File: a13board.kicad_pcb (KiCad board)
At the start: 4 copper layers, 122.3 x 91.1 mm, 147 parts, among them U1 H27UBG8T2A/TSOP48, U2 A13, U3 H5TQ2G43CFR, U4 H5TQ2G43CFR, U5 OLIMEX_IC_AXP209, U6 SY8008BAAC, U7 SY8008BAAC

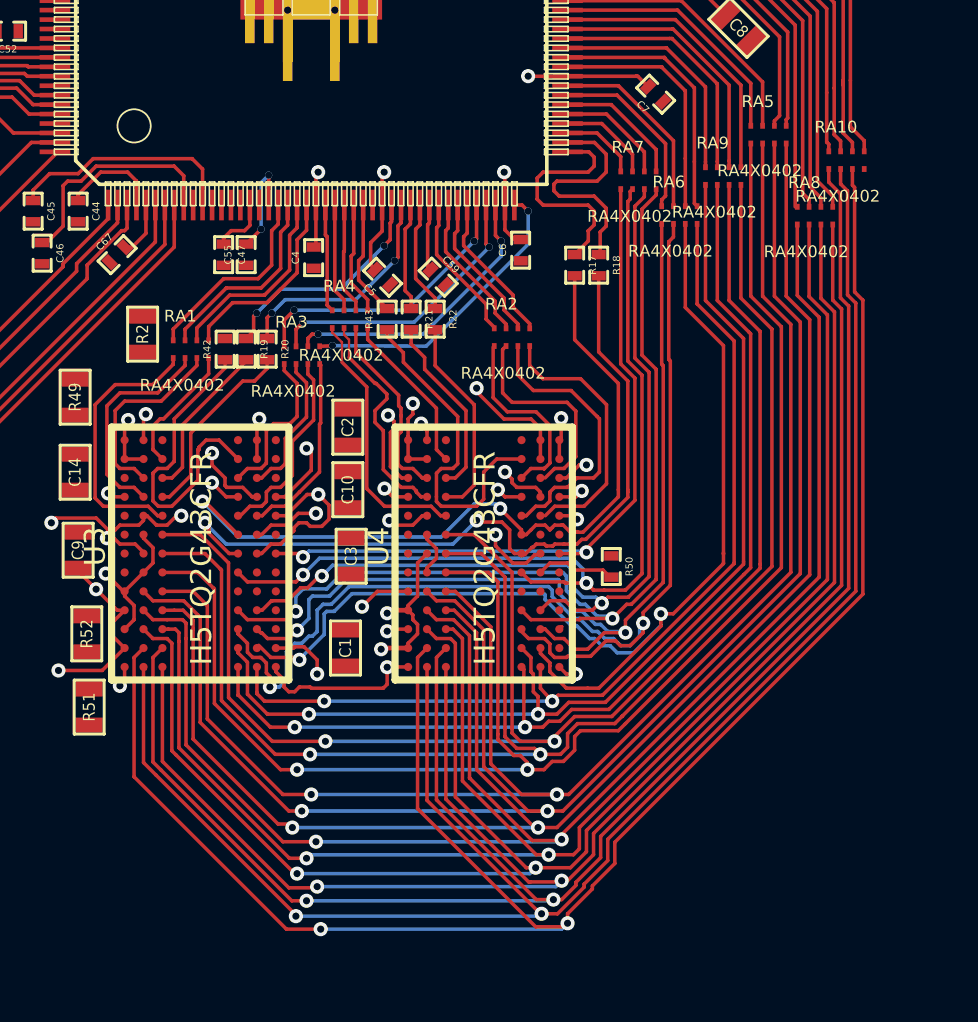
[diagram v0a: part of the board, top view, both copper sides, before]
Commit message: reducing space, occupied by address lines
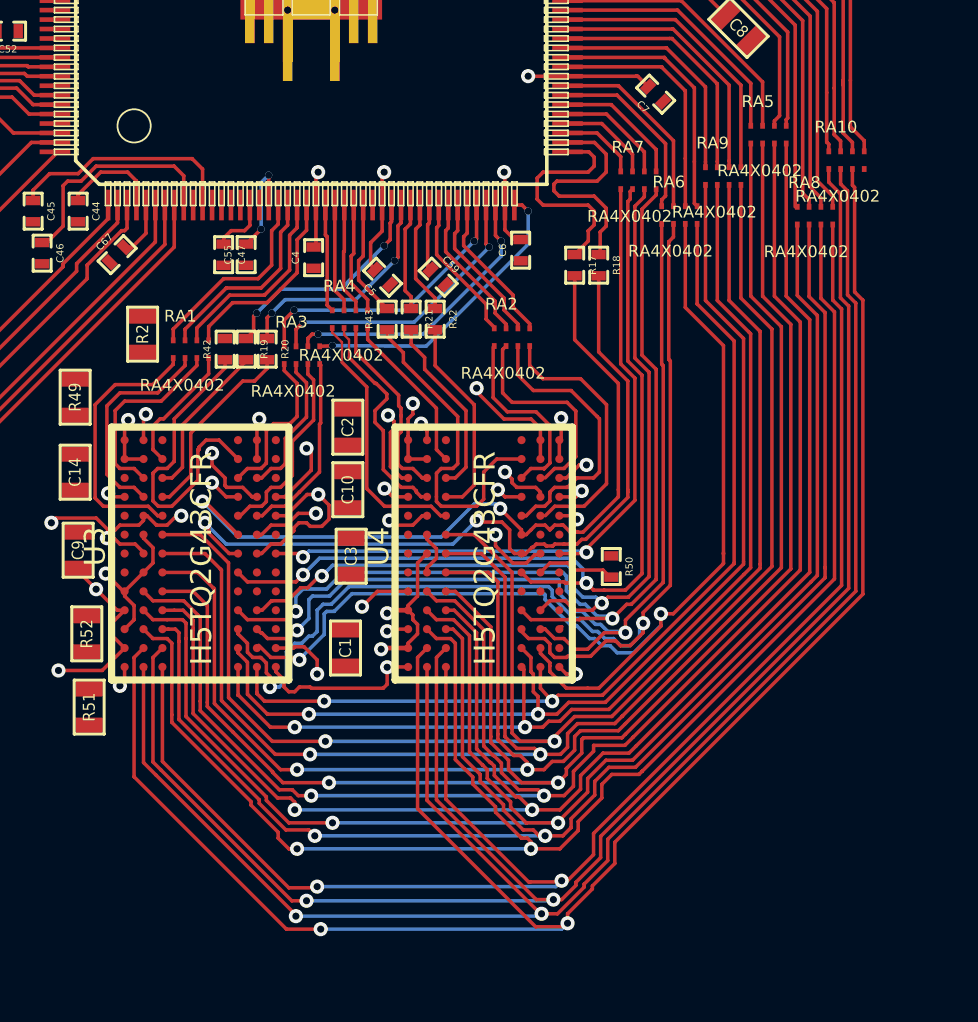
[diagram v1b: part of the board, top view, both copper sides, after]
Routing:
- net /DRAM/DDR3_A2: track 67.6 -> 65.3 mm
- net /DRAM/DDR3_A5: track 69.8 -> 67.6 mm
- net /DRAM/DDR3_A3: track 69.0 -> 67.1 mm
- net /DRAM/DDR3_A0: track 68.5 -> 66.9 mm
- net /DRAM/DDR3_BA0: track 69.4 -> 68.3 mm
- net /DRAM/DDR3_BA2: track 67.2 -> 66.4 mm

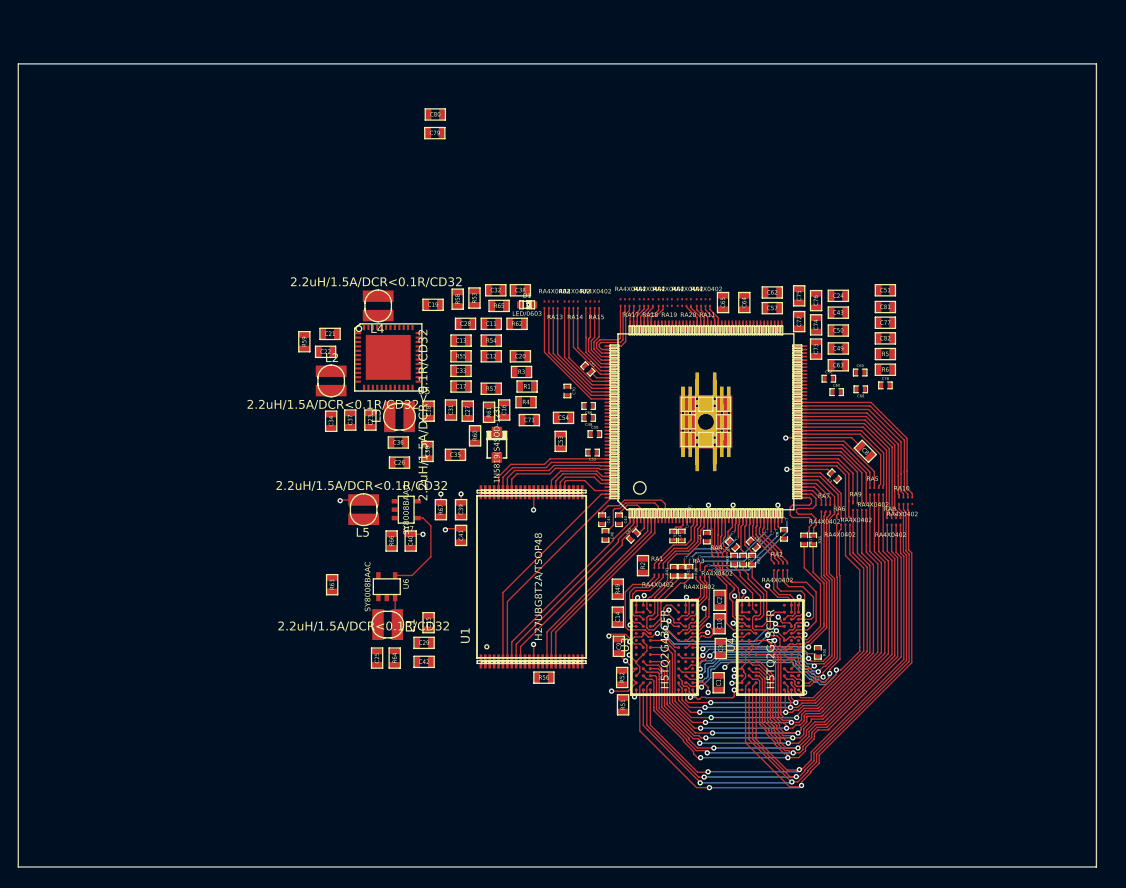
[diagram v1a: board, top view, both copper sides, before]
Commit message: Fixed some bugs with symbols, tracing continued
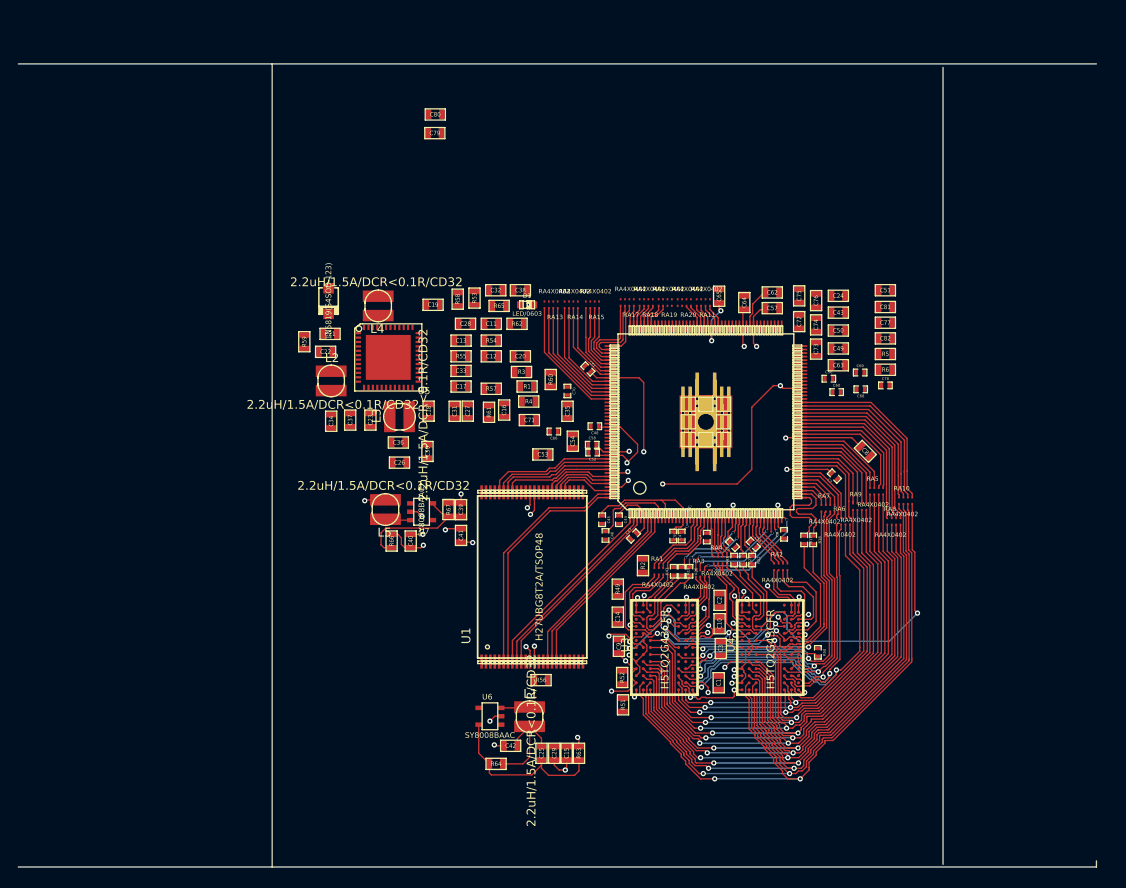
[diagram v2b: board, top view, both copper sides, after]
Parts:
- moved R63 33.9 mm to (99.1, 128.6), turned to 270 degrees
- moved D2 25.1 mm to (70.7, 77.3), turned to 90 degrees
- moved C15 21.6 mm to (97.7, 128.6), turned to 270 degrees
- moved C25 21.6 mm to (94.8, 128.6)
- moved C29 19.4 mm to (96.3, 128.6), turned to 90 degrees
- moved L1 19.2 mm to (93.5, 124.5), turned to 0 degrees
- moved U6 18.8 mm to (89.0, 124.4), turned to 90 degrees
- moved R64 16.6 mm to (89.7, 129.8), turned to 0 degrees
- moved C42 13.7 mm to (91.3, 127.8), turned to 0 degrees
- moved C35 13.6 mm to (97.8, 89.8), turned to 90 degrees
- moved R60 10.7 mm to (95.9, 86.2)
- moved C66 4.90 mm to (96.2, 92.1)
- moved C54 2.85 mm to (98.4, 93.2), turned to 270 degrees
- moved C53 2.51 mm to (95.0, 94.7), turned to 0 degrees
- moved L5 2.47 mm to (77.2, 101.0)
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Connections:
- net N-00000117 renamed /NAND/NRB0
- net N-00000118 renamed /NAND/NDQ6
- net N-00000119 renamed /NAND/NDQ0
- net N-00000121 renamed /NAND/NDQ2
- net N-00000122 renamed /NAND/NDQ4
- net N-00000123 renamed /NAND/NALE
- net N-00000124 renamed /NAND/NRE
- net N-00000128 renamed /NAND/NRB1
- net N-00000132 renamed /NAND/NDQ3
- net N-00000137 renamed /NAND/NDQ1
- net N-00000138 renamed /NAND/NCE1
- net N-00000139 renamed /NAND/NCE0
- net N-00000149 renamed /NAND/NCLE
- net N-00000153 renamed /NAND/NDQ7
- net N-00000159 renamed /NAND/NWE
- net N-00000160 renamed /NAND/NAND_WP
- net N-00000161 renamed /NAND/NDQ5
- net N-00000190 renamed /power/VDD_CPU
- net N-00000191 renamed /power/VDD_INT
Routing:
- net +3.3V: track 4.86 -> 74.2 mm, vias 0 -> 8
- net /DRAM/DDR3_ODT: track 0.00 -> 58.5 mm, vias 0 -> 3
- net /power/VDD_CPU: track 26.3 -> 46.6 mm, vias 0 -> 3
- net N-00000171: track 0.00 -> 20.0 mm
- net GND: track 52.3 -> 67.4 mm, vias 20 -> 27
- net N-00000172: track 0.00 -> 15.1 mm
- net /power/VDD_INT: track 2.82 -> 13.9 mm, vias 0 -> 2
- net RESET_SW: track 10.3 -> 0.00 mm
- net /NAND/NRB0: track 23.6 -> 26.5 mm
- net N-00000169: track 0.00 -> 2.87 mm
- net /DRAM/DDR3_A7: track 79.5 -> 76.8 mm
- net /NAND/NRB1: track 24.6 -> 27.2 mm
- net /DRAM/DDR3_RST: track 74.0 -> 71.7 mm
- net /DRAM/DDR3_A13: track 68.2 -> 66.0 mm
- net /DRAM/DDR3_A9: track 74.3 -> 72.3 mm
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- added copper zone on Inner1.Cu, net +3.3V
- added copper zone on Inner1.Cu, net /power/VDD_CPU
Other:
- outline, holes or cut-outs redrawn

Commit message: Added connectors
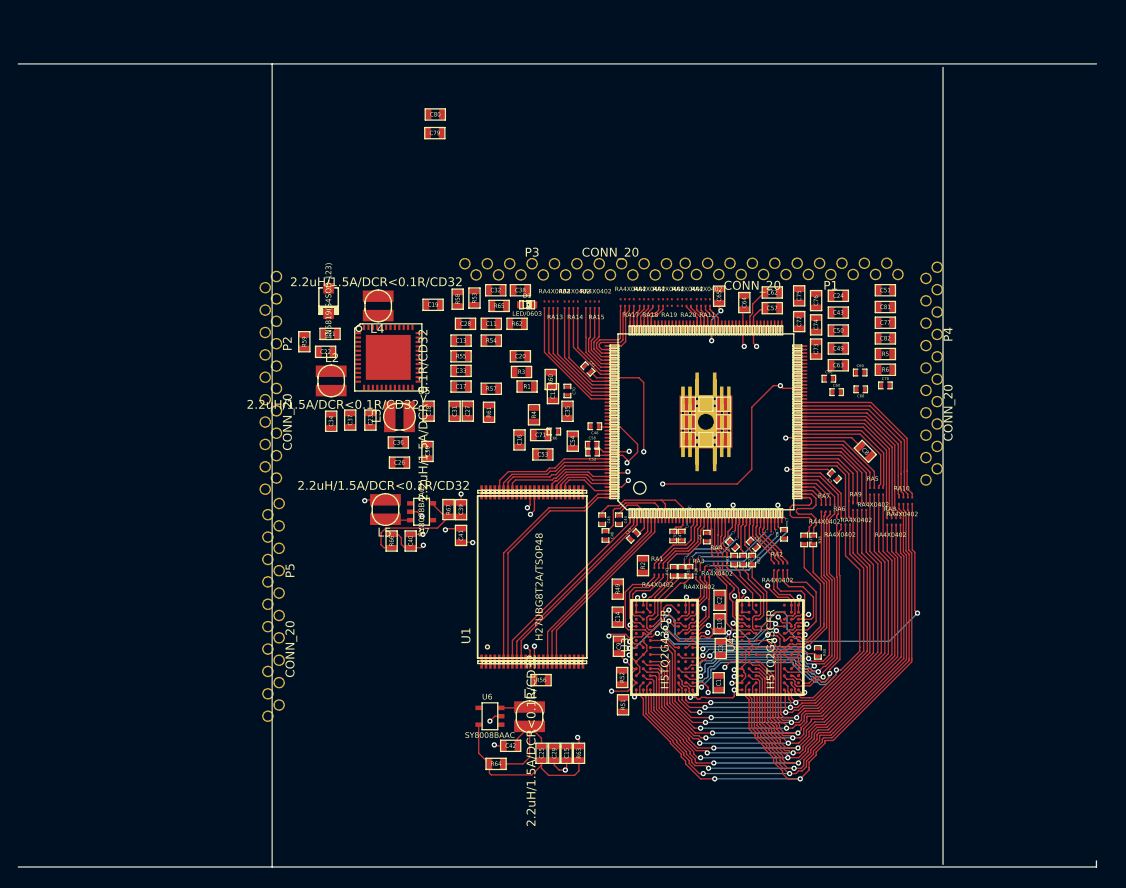
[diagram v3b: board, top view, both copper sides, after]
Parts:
- added P1: CONN_20, CONN20-2.54zzz, F.Cu at (122.0, 73.7)
- added P2: CONN_20, CONN20-2.54zzz, F.Cu at (64.2, 87.8)
- added P3: CONN_20, CONN20-2.54zzz, F.Cu at (99.5, 73.7)
- added P4: CONN_20, CONN20-2.54zzz, F.Cu at (139.1, 86.8)
- added P5: CONN_20, CONN20-2.54zzz, F.Cu at (64.5, 113.6)
- moved C12 8.18 mm to (96.2, 87.8), turned to 270 degrees
- moved C16 3.81 mm to (92.3, 93.0)
- moved C71 2.12 mm to (94.8, 92.5), turned to 0 degrees
- moved R4 1.62 mm to (94.0, 90.2), turned to 270 degrees

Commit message: Meeting 5x10 goal
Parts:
- moved P5 65.9 mm to (125.0, 139.4), turned to 180 degrees
- moved C28 40.1 mm to (120.5, 59.1), turned to 90 degrees
- moved C21 39.5 mm to (104.8, 60.8), turned to 270 degrees
- moved C22 38.7 mm to (104.1, 64.1)
- moved C41 38.2 mm to (99.5, 139.6)
- moved C40 37.5 mm to (93.8, 139.4)
- moved L5 37.5 mm to (90.9, 135.8)
- moved R66 37.5 mm to (91.6, 139.4)
- moved R67 37.5 mm to (98.0, 135.8)
- moved U7 37.5 mm to (95.0, 136.1)
- moved C39 37.5 mm to (99.5, 135.8)
- moved C33 37.4 mm to (120.2, 70.5)
- moved U5 37.4 mm to (110.2, 65.7)
- moved C13 37.4 mm to (120.2, 67.2)
- moved L4 36.8 mm to (107.3, 58.0), turned to 90 degrees
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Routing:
- net RESET_SW: track 0.00 -> 157.4 mm, vias 0 -> 5
- net EXTEN: track 0.00 -> 108.0 mm, vias 0 -> 2
- net USB0-DRV: track 0.00 -> 107.9 mm, vias 0 -> 5
- net PIN2: track 0.00 -> 107.5 mm, vias 0 -> 5
- net VPP: track 0.00 -> 65.0 mm, vias 0 -> 6
- net /power/VDD_INT: track 13.9 -> 66.7 mm, vias 2 -> 6
- net GND: track 67.4 -> 113.2 mm, vias 27 -> 32
- net TWI0_SCK: track 0.00 -> 45.6 mm, vias 0 -> 4
- net TWI0_SDA: track 0.00 -> 40.7 mm, vias 0 -> 4
- net PD14: track 0.00 -> 33.2 mm
- net PD15: track 0.00 -> 32.8 mm
- net PD12: track 0.00 -> 31.2 mm
- net PD13: track 0.00 -> 30.9 mm
- net PD10: track 0.00 -> 28.9 mm
- net PD2: track 0.00 -> 28.6 mm
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- added copper zone on F.Cu, net GND
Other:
- board size 122.3 x 91.1 mm -> 123.5 x 91.1 mm
- net class power: clearance 2 -> 0.2; trace_width 0.2 -> 0.4
- rule solder_mask_min_width: 0.1 -> 0.3

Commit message: A bit more of tracing of PCB
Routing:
- net VMEM: track 105.6 -> 113.4 mm, vias 27 -> 28
- net GND: track 113.2 -> 118.9 mm

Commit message: a bit improved layout
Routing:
- net /DRAM/DDR3_A12: track 42.0 -> 47.2 mm
- net /DRAM/DDR3_A1: track 48.5 -> 50.4 mm
- net /DRAM/DDR3_A4: track 40.7 -> 41.6 mm

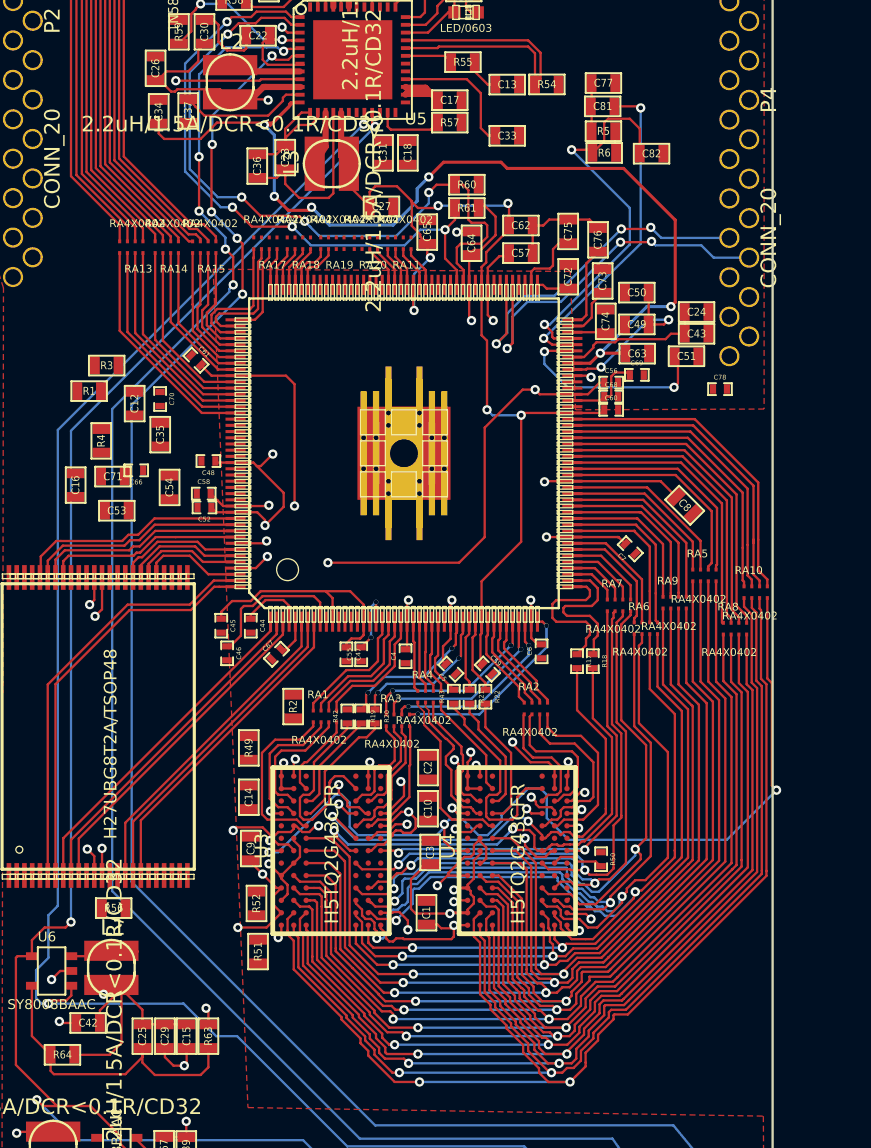
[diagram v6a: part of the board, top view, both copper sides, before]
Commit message: Almost all escaped from BGA
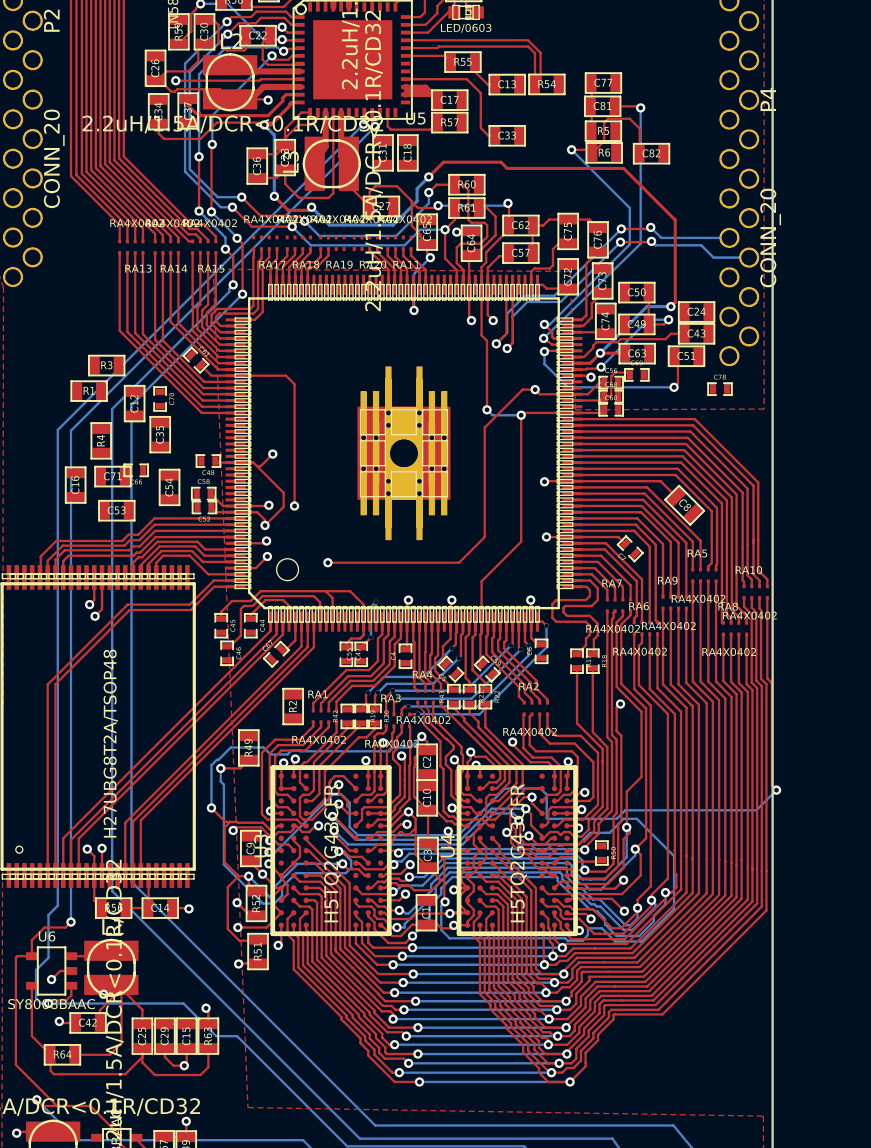
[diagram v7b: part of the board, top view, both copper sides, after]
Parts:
- moved C14 9.14 mm to (97.8, 120.3), turned to 0 degrees
- moved C10 0.70 mm to (115.0, 113.2)
- moved R50 0.40 mm to (126.2, 116.8)
- moved C2 0.35 mm to (115.0, 110.9)
- moved C3 0.23 mm to (115.0, 116.9)
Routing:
- net N-0000056: track 0.00 -> 99.2 mm, vias 0 -> 6
- net GND: track 119.3 -> 144.8 mm, vias 32 -> 35
- net N-0000052: track 0.00 -> 22.5 mm, vias 0 -> 2
- net VMEM: track 113.4 -> 131.8 mm
- net /DRAM/DDR3_A6: track 47.2 -> 54.1 mm
- net /DRAM/DDR3_A4: track 41.6 -> 47.4 mm
- net /DRAM/DDR3_BA1: track 38.5 -> 44.3 mm
- net /NAND/NAND_WP: track 0.00 -> 3.58 mm
- net /DRAM/DDR3_ODT: track 58.5 -> 56.1 mm
- net /DRAM/DDR3_A1: track 50.4 -> 52.7 mm
- net +3.3V: track 81.2 -> 83.5 mm
- net (no net): track 0.00 -> 1.71 mm, vias 0 -> 1
- net /DRAM/DDR3_BA2: track 66.4 -> 67.8 mm
- net /DRAM/DDR3_A14: track 45.7 -> 47.0 mm
- net /DRAM/DDR3_A7: track 76.8 -> 78.1 mm
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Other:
- net class bga: trace_width 0.1016 -> 0.15
- rule trace_min: 0.1016 -> 0.15
- rule via_min_size: 0.6 -> 0.3
